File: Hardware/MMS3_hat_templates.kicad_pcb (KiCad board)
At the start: 2 copper layers, 100 x 50 mm, 29 parts, among them CN401 XT60PW-M, J201 Chainbus in, J202 Chainbus Out, J301 Conn_01x04_Pin, U101 AMS1117, U302 SN74CB3Q3245PWR, U401 XT60PW-F_C428722, U501 M24C64

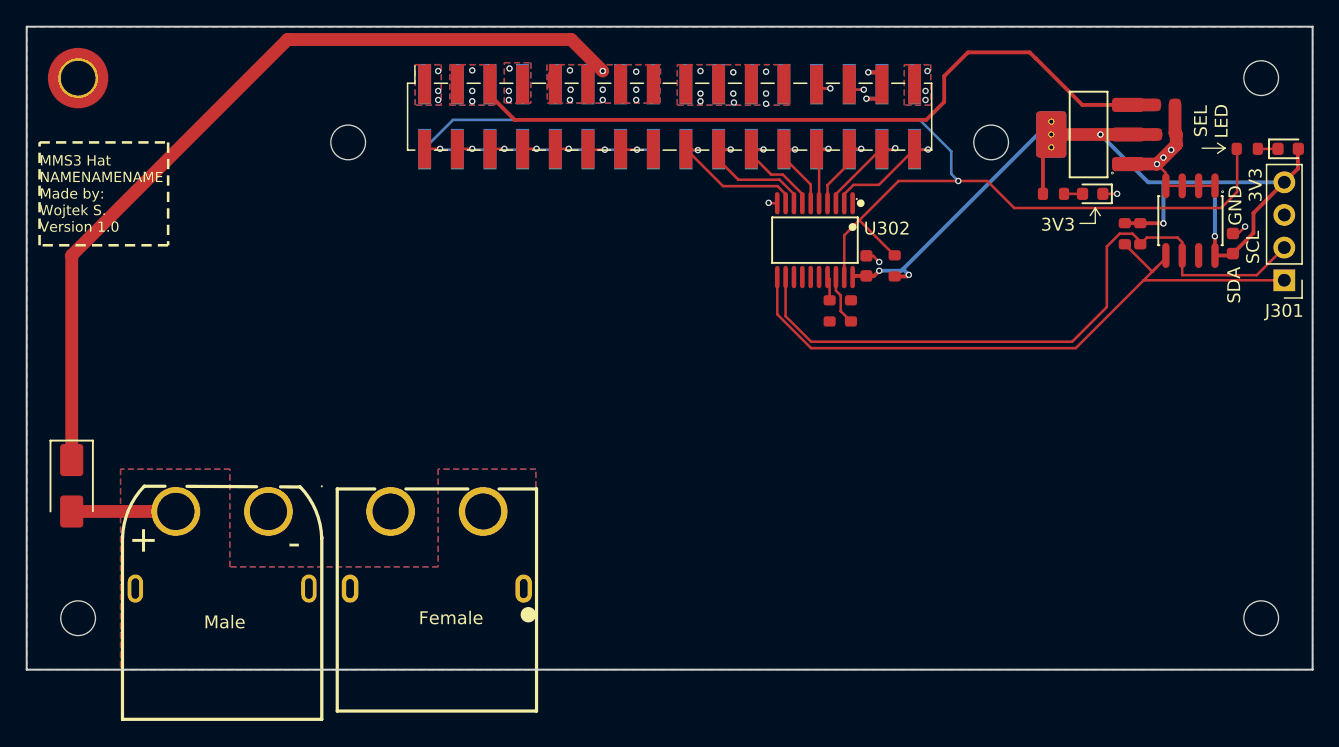
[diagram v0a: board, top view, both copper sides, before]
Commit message: removed I2C connector, added VIN led
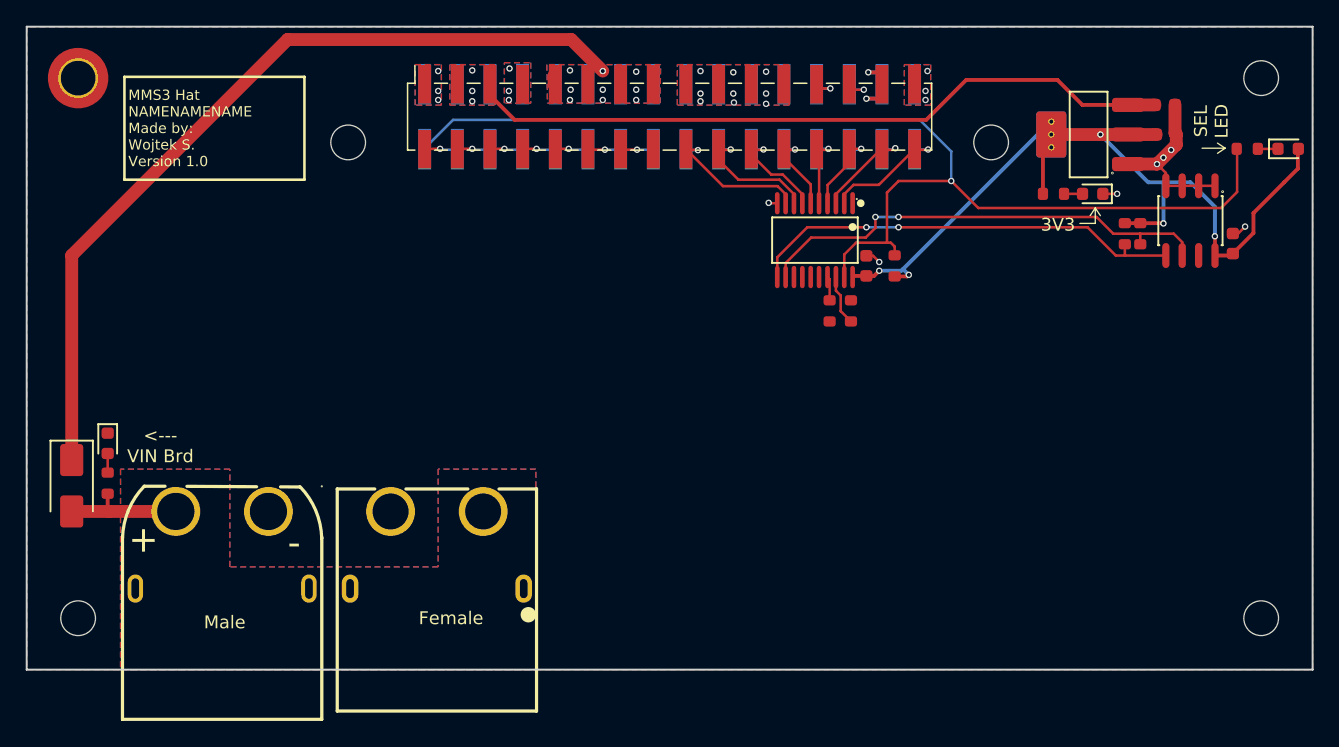
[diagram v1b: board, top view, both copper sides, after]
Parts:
- removed J301: Conn_01x04_Pin, Connector_PinHeader_2.54mm:PinHeader_1x04_P2.54mm_Vertical
- added D402: Red, PCM_JLCPCB:D_0603, F.Cu at (86.3, 122.4)
- added R401: 27kΩ, PCM_JLCPCB:R_0603, F.Cu at (86.3, 125.5)
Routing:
- net /Bus_switch/Chainbus.SDA: track 51.8 -> 34.7 mm, vias 0 -> 2
- net /Bus_switch/Chainbus.SCL: track 53.2 -> 36.6 mm, vias 0 -> 2
- net +3V3: track 74.7 -> 68.2 mm
- net +5V: track 58.4 -> 55.4 mm
- net Net-(D402-Pad2): track 0.00 -> 1.49 mm
- net /Power Connector/VIN_BRD: track 8.10 -> 9.52 mm
- net /Bus_switch/SEL1: track 89.7 -> 88.5 mm
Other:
- board text added: "<--- VIN Brd"
- board text removed: "GND"
- board text removed: "SCL"
- board text removed: "SDA"

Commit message: connected #WC to GND
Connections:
- U501 pad 7: unconnected-(U501-#WC-Pad7) -> GND
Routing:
- net GND: track 17.5 -> 19.0 mm, vias 25 -> 26
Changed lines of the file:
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@@
 			(size 0.57 1.95)
 			(layers "F.Cu" "F.Mask" "F.Paste")
-			(net "unconnected-(U501-#WC-Pad7)")
+			(net "GND")
 			(pinfunction "#WC_7")
-			(pintype "unspecified+no_connect")
+			(pintype "unspecified")
 		)
 		(pad "8" smd oval
@@
 	)
 	(segment
+		(start 171.14 106.34)
+		(end 171.1 106.3)
+		(width 0.2)
+		(layer "F.Cu")
+		(net "GND")
+	)
+	(segment
+		(start 171.14 107.795)
+		(end 171.14 106.34)
+		(width 0.2)
+		(layer "F.Cu")
+		(net "GND")
+	)
+	(segment
 		(start 138.37 103.73)
 		(end 137.73 103.73)
@@
 		(size 0.5)
 		(drill 0.3)
+		(layers "F.Cu" "B.Cu")
+		(net "GND")
+	)
+	(via
+		(at 171.1 106.3)
+		(size 0.5)
+		(drill 0.3)

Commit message: added PCB radiator to LDO
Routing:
- added copper zone on B.Cu, net +3V3
